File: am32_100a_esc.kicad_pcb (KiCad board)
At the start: 4 copper layers, 0 parts

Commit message: ROUTING COMPLETE
Read for production. With Gerber
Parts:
- added A: MOTORA, MountingHole:MountingHole_3.7mm_Pad_Via, F.Cu at (182.1, 84.9)
- added B: MOTORB, MountingHole:MountingHole_3.7mm_Pad_Via, F.Cu at (182.2, 96.0)
- added C: MOTORC, MountingHole:MountingHole_3.7mm_Pad_Via, F.Cu at (182.1, 107.2)
- added C1: 0.1uf, Capacitor_SMD:C_0603_1608Metric, F.Cu at (121.1, 86.0)
- added C2: 0.33uf, Capacitor_SMD:C_0603_1608Metric, B.Cu at (127.0, 111.1)
- added C32: 100 nf, Capacitor_SMD:C_0603_1608Metric, B.Cu at (138.4, 106.8)
- added C33: 100 nf, Capacitor_SMD:C_0603_1608Metric, B.Cu at (140.0, 106.8)
- added C34: 10uf, Capacitor_SMD:C_0603_1608Metric, F.Cu at (108.3, 95.0)
- added C35: 100nf, Capacitor_SMD:C_0603_1608Metric, F.Cu at (108.3, 96.5)
- added C36: 1uf, Capacitor_SMD:C_1206_3216Metric, F.Cu at (123.7, 92.2)
- added C37: 1uf, Capacitor_SMD:C_1206_3216Metric, F.Cu at (127.3, 95.1)
- added C38: 1uf, Capacitor_SMD:C_1206_3216Metric, F.Cu at (127.1, 100.8)
- added C39: 0.33uf, Capacitor_SMD:C_0805_2012Metric, F.Cu at (160.9, 112.9)
- added C40: 0.1uf, Capacitor_SMD:C_0402_1005Metric, F.Cu at (172.2, 112.5)
- added C41: 0.33uf, Capacitor_SMD:C_0805_2012Metric, B.Cu at (123.9, 110.4)
- added C42: 100nf, Capacitor_SMD:C_0402_1005Metric, B.Cu at (123.1, 106.9)
- added C43: 2.2uf, Capacitor_SMD:C_0603_1608Metric, F.Cu at (112.6, 84.0)
- added C44: 470pf, Capacitor_SMD:C_0603_1608Metric, F.Cu at (117.4, 86.3)
- added C54: 22uf, Capacitor_SMD:C_1210_3225Metric, B.Cu at (113.1, 107.8)
- added C55: 22uf, Capacitor_SMD:C_1210_3225Metric, B.Cu at (113.1, 112.5)
- added C56: 22uf, Capacitor_SMD:C_1210_3225Metric, B.Cu at (116.4, 112.5)
- added C57: 10uf, Capacitor_SMD:C_0603_1608Metric, F.Cu at (119.2, 91.7)
- added C58: 100nf, Capacitor_SMD:C_0603_1608Metric, F.Cu at (119.2, 90.2)
- added C59: 100nf, Capacitor_SMD:C_0603_1608Metric, B.Cu at (122.6, 97.0)
- added C60: 100nf, Capacitor_SMD:C_0603_1608Metric, F.Cu at (119.2, 88.7)
- added C61: 1uf, Capacitor_SMD:C_0603_1608Metric, B.Cu at (130.4, 96.4)
- added C62: 10nf, Capacitor_SMD:C_0603_1608Metric, B.Cu at (130.4, 94.8)
- added C63: 22uf, Capacitor_SMD:C_1210_3225Metric, B.Cu at (116.4, 107.8)
- added C64: 22uf, Capacitor_SMD:C_1210_3225Metric, B.Cu at (119.7, 107.8)
- added C65: 22uf, Capacitor_SMD:C_1210_3225Metric, B.Cu at (119.7, 112.5)
- added D2: SS23, Diode_SMD:D_SMA, F.Cu at (117.3, 81.8)
- added G***: LOGO, graphics:nervous-frog, B.Cu at (175.6, 113.5)
- added G***: LOGO, graphics:nervous-frog, B.Cu at (168.6, 113.5)
- added G***: LOGO, graphics:nervous-frog, B.Cu at (147.6, 79.8)
- added G***: LOGO, graphics:nervous-frog, B.Cu at (175.6, 101.7)
- added G***: LOGO, graphics:nervous-frog, B.Cu at (147.6, 90.5)
- added G***: LOGO, graphics:nervous-frog, B.Cu at (154.6, 90.5)
- added G***: LOGO, graphics:nervous-frog, B.Cu at (161.6, 90.5)
- added G***: LOGO, graphics:nervous-frog, B.Cu at (147.6, 113.5)
- added G***: LOGO, graphics2:pookie, B.Cu at (125.5, 93.3)
- added G***: LOGO, graphics:nervous-frog, B.Cu at (161.6, 79.8)
- added G***: LOGO, graphics:nervous-frog, B.Cu at (161.6, 101.7)
- added G***: LOGO, graphics:nervous-frog, B.Cu at (175.6, 79.8)
- added G***: LOGO, graphics:nervous-frog, B.Cu at (161.6, 113.5)
- added G***: LOGO, graphics:nervous-frog, B.Cu at (154.6, 113.5)
- added G***: LOGO, graphics:nervous-frog, B.Cu at (147.6, 101.7)
- added G***: LOGO, graphics:nervous-frog, B.Cu at (154.6, 79.8)
- added G***: LOGO, graphics:nervous-frog, B.Cu at (168.6, 101.7)
- added G***: LOGO, graphics:nervous-frog, B.Cu at (175.6, 90.5)
- added G***: LOGO, graphics:nervous-frog, B.Cu at (168.6, 79.8)
- added G***: LOGO, graphics:nervous-frog, B.Cu at (154.6, 101.7)
- added G***: LOGO, graphics:nervous-frog, B.Cu at (168.6, 90.5)
- added H4: BATT+, MountingHole:MountingHole_4.3mm_M4_Pad_Via, F.Cu at (131.6, 83.3)
- added H5: GND, MountingHole:MountingHole_4.3mm_M4_Pad_Via, F.Cu at (132.8, 109.3)
- added IC5: DRV8300DPWR, DRV8300DPWR:SOP65P640X120-20N, F.Cu at (116.6, 98.6)
- added IC6: AS78L05RTR-G1, AS78L05RTR-G1:ZXTP19060CZTA, F.Cu at (168.4, 114.0)
- added IC7: L7805ACD2T-TR, Package_TO_SOT_SMD:TO-263-2, F.Cu at (117.9, 109.4)
- added IC8: MIC5209-3.3YM-TR, MIC5209-3.3YM-TR:SOIC127P599X173-8N, F.Cu at (123.3, 80.6)
- added J1: Conn_01x03_Pin, Connector_PinHeader_2.54mm:PinHeader_1x03_P2.54mm_Vertical, F.Cu at (109.6, 108.2)
- added J2: Conn_01x02_Pin, Connector_PinHeader_2.54mm:PinHeader_1x02_P2.54mm_Vertical, F.Cu at (109.2, 78.5)
- added J3: Conn_01x01_Pin, custom_components:capacitor_hole_custom, F.Cu at (136.2, 78.5)
- added J4: Conn_01x04_Pin, Connector_PinHeader_2.54mm:PinHeader_1x04_P2.54mm_Vertical, F.Cu at (108.4, 84.7)
- added J5: Conn_01x01_Pin, custom_components:capacitor_hole_custom, F.Cu at (130.8, 92.2)
- added J6: Conn_01x01_Pin, custom_components:capacitor_hole_custom, F.Cu at (136.9, 115.5)
- added J7: Conn_01x01_Pin, custom_components:capacitor_hole_custom, F.Cu at (129.4, 115.5)
- added LED1: SML-D12U1WT86, SML-D12U1WT86:LEDC1608X65N, F.Cu at (164.1, 113.1)
- added Q13: TPH1R204PB,L1Q, TPH1R204PB,L1Q:TPH1R306PLL1Q, F.Cu at (154.9, 85.8)
- added Q14: TPH1R204PB,L1Q, TPH1R204PB,L1Q:TPH1R306PLL1Q, F.Cu at (171.5, 95.1)
- added Q15: TPH1R204PB,L1Q, TPH1R204PB,L1Q:TPH1R306PLL1Q, F.Cu at (146.7, 108.2)
- added Q16: TPH1R204PB,L1Q, TPH1R204PB,L1Q:TPH1R306PLL1Q, F.Cu at (146.7, 85.8)
- added Q17: TPH1R204PB,L1Q, TPH1R204PB,L1Q:TPH1R306PLL1Q, F.Cu at (163.2, 95.1)
- added Q18: TPH1R204PB,L1Q, TPH1R204PB,L1Q:TPH1R306PLL1Q, F.Cu at (154.9, 108.2)
- added Q19: TPH1R204PB,L1Q, TPH1R204PB,L1Q:TPH1R306PLL1Q, F.Cu at (163.2, 83.9)
- added Q20: TPH1R204PB,L1Q, TPH1R204PB,L1Q:TPH1R306PLL1Q, F.Cu at (146.7, 97.0)
- added Q21: TPH1R204PB,L1Q, TPH1R204PB,L1Q:TPH1R306PLL1Q, F.Cu at (163.2, 106.3)
- added Q22: TPH1R204PB,L1Q, TPH1R204PB,L1Q:TPH1R306PLL1Q, F.Cu at (171.5, 83.9)
- added Q23: TPH1R204PB,L1Q, TPH1R204PB,L1Q:TPH1R306PLL1Q, F.Cu at (154.9, 97.0)
- added Q24: TPH1R204PB,L1Q, TPH1R204PB,L1Q:TPH1R306PLL1Q, F.Cu at (171.5, 106.3)
- added R31: 5Ω, Resistor_SMD:R_0402_1005Metric, F.Cu at (159.0, 88.6)
- added R32: 5Ω, Resistor_SMD:R_0402_1005Metric, F.Cu at (167.4, 92.3)
- added R33: 5Ω, Resistor_SMD:R_0402_1005Metric, F.Cu at (150.8, 110.9)
- added R34: 5Ω, Resistor_SMD:R_0402_1005Metric, F.Cu at (150.8, 88.8)
- added R35: 5Ω, Resistor_SMD:R_0402_1005Metric, F.Cu at (159.1, 92.4)
- added R36: 5Ω, Resistor_SMD:R_0402_1005Metric, F.Cu at (159.0, 111.1)
- added R37: 5Ω, Resistor_SMD:R_0402_1005Metric, F.Cu at (159.1, 81.1)
- added R38: 5Ω, Resistor_SMD:R_0402_1005Metric, F.Cu at (150.8, 99.9)
- added R39: 5Ω, Resistor_SMD:R_0402_1005Metric, F.Cu at (159.2, 103.3)
- added R40: 5Ω, Resistor_SMD:R_0402_1005Metric, F.Cu at (167.3, 81.1)
- added R41: 5Ω, Resistor_SMD:R_0402_1005Metric, F.Cu at (159.1, 99.8)
- added R42: 5Ω, Resistor_SMD:R_0402_1005Metric, F.Cu at (167.4, 103.3)
- added R43: LRMAP3920C-R001FT, LRMAP3920C-R001FT:RESC10052X136N, B.Cu at (135.3, 101.0)
- added R44: 1k, Resistor_SMD:R_0402_1005Metric, B.Cu at (137.1, 105.6)
- added R45: 10k, Resistor_SMD:R_0402_1005Metric, F.Cu at (176.4, 90.2)
- added R46: 1k, Resistor_SMD:R_0402_1005Metric, F.Cu at (176.4, 91.9)
- added R47: 10k, Resistor_SMD:R_0402_1005Metric, F.Cu at (176.0, 88.6)
- added R48: 10k, Resistor_SMD:R_0402_1005Metric, F.Cu at (176.3, 103.4)
- added R49: 1k, Resistor_SMD:R_0402_1005Metric, F.Cu at (176.4, 101.3)
- added R50: 10k, Resistor_SMD:R_0402_1005Metric, F.Cu at (175.8, 99.8)
- added R51: 10k, Resistor_SMD:R_0402_1005Metric, F.Cu at (176.7, 112.0)
- added R52: 1k, Resistor_SMD:R_0402_1005Metric, F.Cu at (174.5, 112.0)
- added R53: 10k, Resistor_SMD:R_0402_1005Metric, F.Cu at (175.6, 110.9)
- added R54: 100k, Resistor_SMD:R_0603_1608Metric, F.Cu at (136.9, 94.4)
- added R55: 10k, Resistor_SMD:R_0603_1608Metric, B.Cu at (136.9, 96.0)
- added R56: 140, Resistor_SMD:R_0402_1005Metric, F.Cu at (163.9, 115.4)
- added R59: 10k, Resistor_SMD:R_0402_1005Metric, B.Cu at (118.3, 92.6)
- added R60: 1K, Resistor_SMD:R_0402_1005Metric, F.Cu at (109.3, 105.4)
- added U2: L7809, Package_TO_SOT_SMD:TO-263-2, B.Cu at (116.7, 86.0)
- added U4: INA180B2, Package_TO_SOT_SMD:SOT-23-5, F.Cu at (135.4, 103.1)
- added U6: STM32F051C8Ux, Package_DFN_QFN:QFN-48-1EP_7x7mm_P0.5mm_EP5.6x5.6mm, B.Cu at (117.3, 98.0)
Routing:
- net GND: track 0.00 -> 313.4 mm, vias 0 -> 48
- net BEMF_COMMON: track 0.00 -> 158.0 mm, vias 0 -> 2
- net LOW_SIDE_SOURCE: track 0.00 -> 137.2 mm, vias 0 -> 48
- net BATT+: track 0.00 -> 127.7 mm, vias 0 -> 48
- net BEMFA: track 0.00 -> 108.6 mm, vias 0 -> 2
- net BEMFB: track 0.00 -> 107.3 mm, vias 0 -> 2
- net +3.3V: track 0.00 -> 101.3 mm, vias 0 -> 6
- net BEMFC: track 0.00 -> 71.6 mm, vias 0 -> 2
- net GLC: track 0.00 -> 69.8 mm, vias 0 -> 5
- net GLA: track 0.00 -> 65.3 mm, vias 0 -> 3
- net GLB: track 0.00 -> 61.9 mm, vias 0 -> 5
- net MOTORA: track 0.00 -> 54.1 mm, vias 0 -> 85
- net GHB: track 0.00 -> 53.5 mm, vias 0 -> 3
- net MOTORC: track 0.00 -> 52.8 mm, vias 0 -> 85
- net MOTORB: track 0.00 -> 49.3 mm, vias 0 -> 85
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- added copper zone on B.Cu, net GND
- added copper zone on F.Cu, net GND
- added copper zone on In1.Cu, net GND
- added copper zone on In2.Cu, net GND
- added copper zone on B.Cu, net LOW_SIDE_SOURCE
- added copper zone on F.Cu, net LOW_SIDE_SOURCE
- added copper zone on In1.Cu, net LOW_SIDE_SOURCE
- added copper zone on In2.Cu, net LOW_SIDE_SOURCE
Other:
- board outline added: 84 x 41 mm
- board text added: "+"
- board text added: "-"
- board text added: "3.3v"
- board text added: "A"
- board text added: "B"
- board text added: "BATT+"
- board text added: "C"
- board text added: "D"
- board text added: "Designed by HOOMAN"
- board text added: "G"
- board text added: "GND"
- board text added: "HOW ?"
- board text added: "S"
- board text added: "TX"
- board text added: "TY"
- board text added: "WHY ?"

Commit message: added more doodles
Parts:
- removed the G*** at (125.5, 93.3)
- added G***: LOGO, graphics:runn, F.Cu at (141.7, 90.8)
- added G***: LOGO, graphics:pookie, B.Cu at (125.5, 94.5)
- added G***: LOGO, graphics:hidding_cat, B.Cu at (143.1, 96.0)
- added G***: LOGO, graphics:runn, F.Cu at (141.7, 101.9)
- added G***: LOGO, graphics:hidding_cat, B.Cu at (143.1, 84.8)
- added G***: LOGO, graphics:hidding_cat, B.Cu at (143.1, 107.2)
- renumbered J3 to BATT+, H4 to BATT+, J6 to BATT+, J7 to GND, H5 to GND, J5 to GND
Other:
- board text added: "Designed by HOOMAN‍️"
- board text removed: "Designed by HOOMAN"

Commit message: Final from my side with drc checked .
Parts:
- C1, C40: value 0.1uf -> 100nf
- C2, C39, C41: value 0.33uf -> 330nf
- C32, C33: value 100 nf -> 100nf
- C54, C55, C56, C63, C64, C65: value 22uf -> 4.7uf
- R31, R32, R33, R34, R35, R36, R37, R38, R39, R40, R41, R42: value 5Ω -> 5.1
- renumbered A to A1, B to B1, BATT+ to BATT+1, BATT+ to BATT+2, BATT+ to BATT+3, C to C3, GND to GND1, GND to GND2, GND to GND3

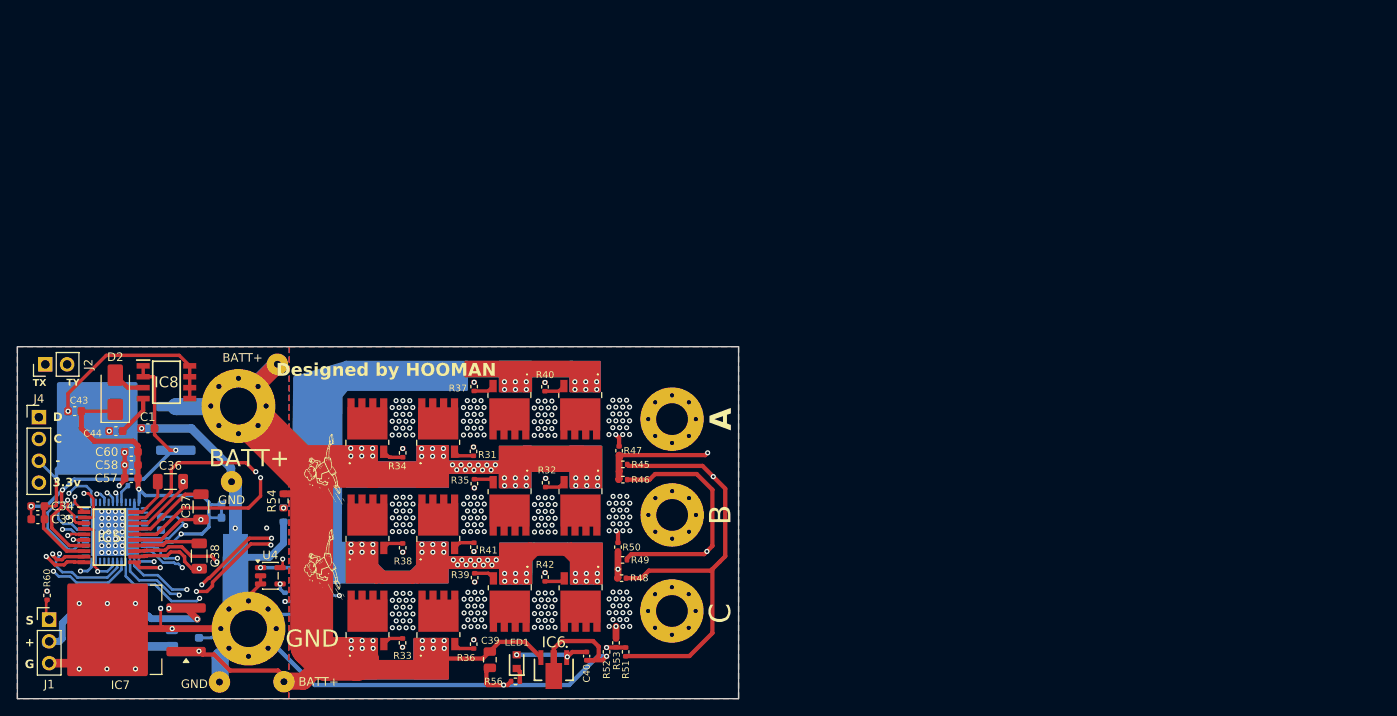
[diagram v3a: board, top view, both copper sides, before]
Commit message: re started with routing for better working and removing wrong connections
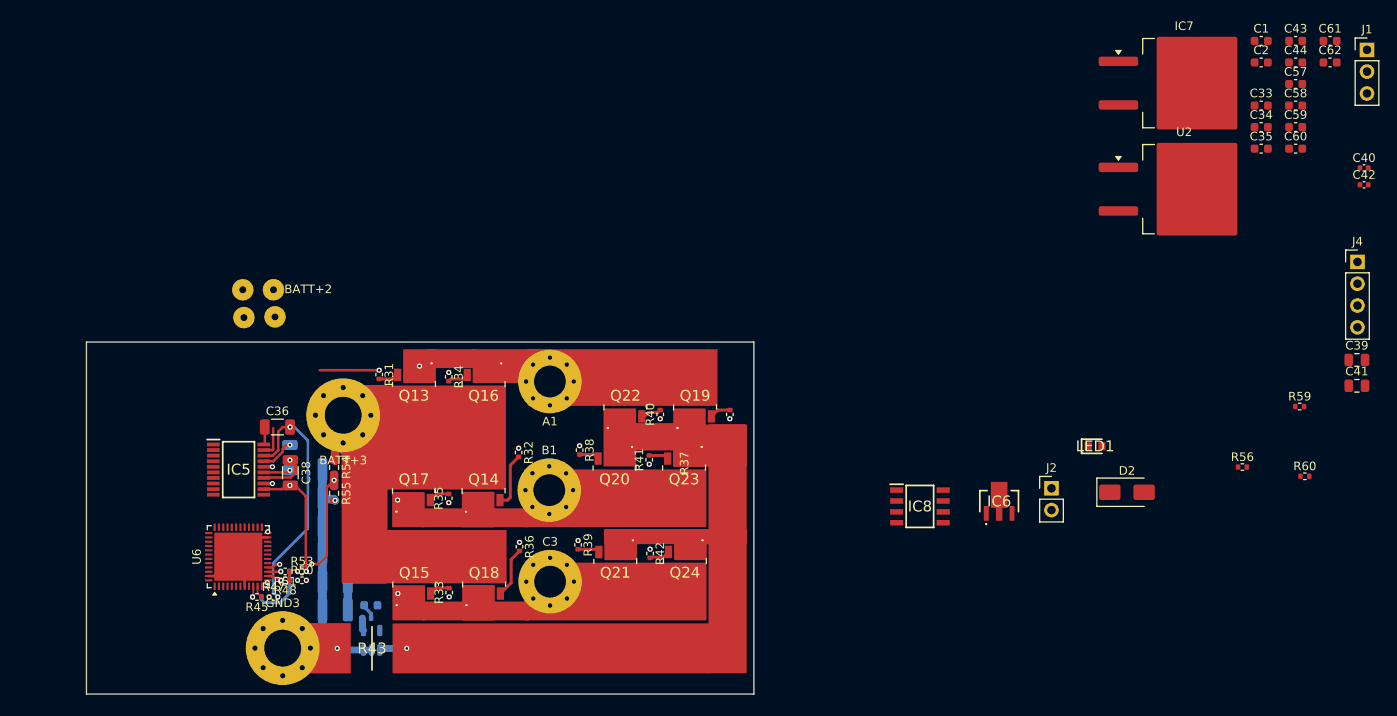
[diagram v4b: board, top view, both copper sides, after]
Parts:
- removed G*** (x2): LOGO, graphics:runn
- removed G*** (x20): LOGO, graphics:nervous-frog
- removed G***: LOGO, graphics:pookie
- removed G*** (x3): LOGO, graphics:hidding_cat
- C2, C33, C41, C42, C59, C61, C62, R43, R55, R59, U2, U6: moved to F.Cu
- C37, R46, R49, R52, U4: moved to B.Cu
- moved J1 167.2 mm to (263.1, 41.9)
- moved J4 154.6 mm to (262.0, 66.6)
- moved C34 149.2 mm to (250.8, 50.9)
- moved C35 148.9 mm to (250.8, 53.4)
- moved C43 148.6 mm to (254.8, 40.8), turned to 0 degrees
- moved C42 148.1 mm to (262.8, 57.6), turned to 0 degrees
- moved R60 147.2 mm to (255.8, 91.5), turned to 0 degrees
- moved C44 144.0 mm to (254.8, 43.3), turned to 0 degrees
- moved C57 143.2 mm to (254.8, 45.8), turned to 0 degrees
- moved C58 141.9 mm to (254.8, 48.4), turned to 0 degrees
- moved C41 141.1 mm to (261.9, 81.0), turned to 0 degrees
- moved C2 141.1 mm to (250.8, 43.3), turned to 0 degrees
- moved C60 140.1 mm to (254.8, 53.4), turned to 0 degrees
- moved C59 140.0 mm to (254.8, 50.9), turned to 0 degrees
- moved C61 139.8 mm to (258.8, 40.8)
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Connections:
- Q13 pad 1: BATT+ -> MOTORA
- Q13 pad 2: BATT+ -> MOTORA
- Q13 pad 3: BATT+ -> MOTORA
- Q13 pad 5: MOTORA -> BATT+
- Q13 pad 6: MOTORA -> BATT+
- Q13 pad 7: MOTORA -> BATT+
- Q13 pad 8: MOTORA -> BATT+
- Q13 pad 9: MOTORA -> BATT+
- Q14 pad 1: BATT+ -> MOTORB
- Q14 pad 2: BATT+ -> MOTORB
- Q14 pad 3: BATT+ -> MOTORB
- Q14 pad 5: MOTORB -> BATT+
- Q14 pad 6: MOTORB -> BATT+
- Q14 pad 7: MOTORB -> BATT+
- Q14 pad 8: MOTORB -> BATT+
- Q14 pad 9: MOTORB -> BATT+
- Q15 pad 1: BATT+ -> MOTORC
- Q15 pad 2: BATT+ -> MOTORC
- Q15 pad 3: BATT+ -> MOTORC
- Q15 pad 5: MOTORC -> BATT+
- Q15 pad 6: MOTORC -> BATT+
- Q15 pad 7: MOTORC -> BATT+
- Q15 pad 8: MOTORC -> BATT+
- Q15 pad 9: MOTORC -> BATT+
- Q16 pad 1: BATT+ -> MOTORA
- Q16 pad 2: BATT+ -> MOTORA
- Q16 pad 3: BATT+ -> MOTORA
- Q16 pad 5: MOTORA -> BATT+
- Q16 pad 6: MOTORA -> BATT+
- Q16 pad 7: MOTORA -> BATT+
- Q16 pad 8: MOTORA -> BATT+
- Q16 pad 9: MOTORA -> BATT+
- Q17 pad 1: BATT+ -> MOTORB
- Q17 pad 2: BATT+ -> MOTORB
- Q17 pad 3: BATT+ -> MOTORB
- Q17 pad 5: MOTORB -> BATT+
- Q17 pad 6: MOTORB -> BATT+
- Q17 pad 7: MOTORB -> BATT+
- Q17 pad 8: MOTORB -> BATT+
- Q17 pad 9: MOTORB -> BATT+
- Q18 pad 1: BATT+ -> MOTORC
- Q18 pad 2: BATT+ -> MOTORC
- Q18 pad 3: BATT+ -> MOTORC
- Q18 pad 5: MOTORC -> BATT+
- Q18 pad 6: MOTORC -> BATT+
- Q18 pad 7: MOTORC -> BATT+
- Q18 pad 8: MOTORC -> BATT+
- Q18 pad 9: MOTORC -> BATT+
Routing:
- net GND: track 313.4 -> 49.3 mm, vias 48 -> 2
- net BEMF_COMMON: track 158.0 -> 2.46 mm, vias 2 -> 0
- net LOW_SIDE_SOURCE: track 137.2 -> 3.17 mm, vias 48 -> 1
- net BEMFA: track 108.6 -> 3.40 mm
- net BEMFB: track 107.3 -> 3.75 mm
- net BATT+: track 127.7 -> 25.3 mm, vias 48 -> 0
- net +3.3V: track 101.3 -> 0.00 mm, vias 6 -> 1
- net BEMFC: track 71.6 -> 3.49 mm
- net GLC: track 69.8 -> 10.3 mm, vias 5 -> 2
- net GLA: track 65.3 -> 9.51 mm, vias 3 -> 2
- net GLB: track 61.9 -> 9.61 mm, vias 5 -> 2
- net +9V: track 43.2 -> 0.00 mm, vias 3 -> 0
- net GHB: track 53.5 -> 13.0 mm
- net MOTORC: track 52.8 -> 14.4 mm, vias 85 -> 3
- net GHC: track 46.3 -> 13.2 mm
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- removed copper zone on B.Cu, net GND
- removed copper zone on F.Cu, net GND
- removed copper zone on In1.Cu, net GND
- removed copper zone on In2.Cu, net GND
- removed copper zone on B.Cu, net LOW_SIDE_SOURCE
- removed copper zone on F.Cu, net LOW_SIDE_SOURCE
- removed copper zone on In1.Cu, net LOW_SIDE_SOURCE
- removed copper zone on In2.Cu, net LOW_SIDE_SOURCE
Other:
- board size 84 x 41 mm -> 77.7 x 41 mm
- board text removed: "+"
- board text removed: "-"
- board text removed: "3.3v"
- board text removed: "A"
- board text removed: "B"
- board text removed: "BATT+"
- board text removed: "C"
- board text removed: "D"
- board text removed: "Designed by HOOMAN‍️"
- board text removed: "G"
- board text removed: "GND"
- board text removed: "HOW ?"
- board text removed: "S"
- board text removed: "TX"
- board text removed: "TY"
- board text removed: "WHY ?"
